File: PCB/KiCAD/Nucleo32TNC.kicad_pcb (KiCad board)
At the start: 2 copper layers, 66 x 99 mm, 54 parts, among them J1 SJ-43515TS, Q1 2N7000, Q2 2N7000, SW1 PTS645VL58-2 LFS, U1 MCP6004, U2 24LC32

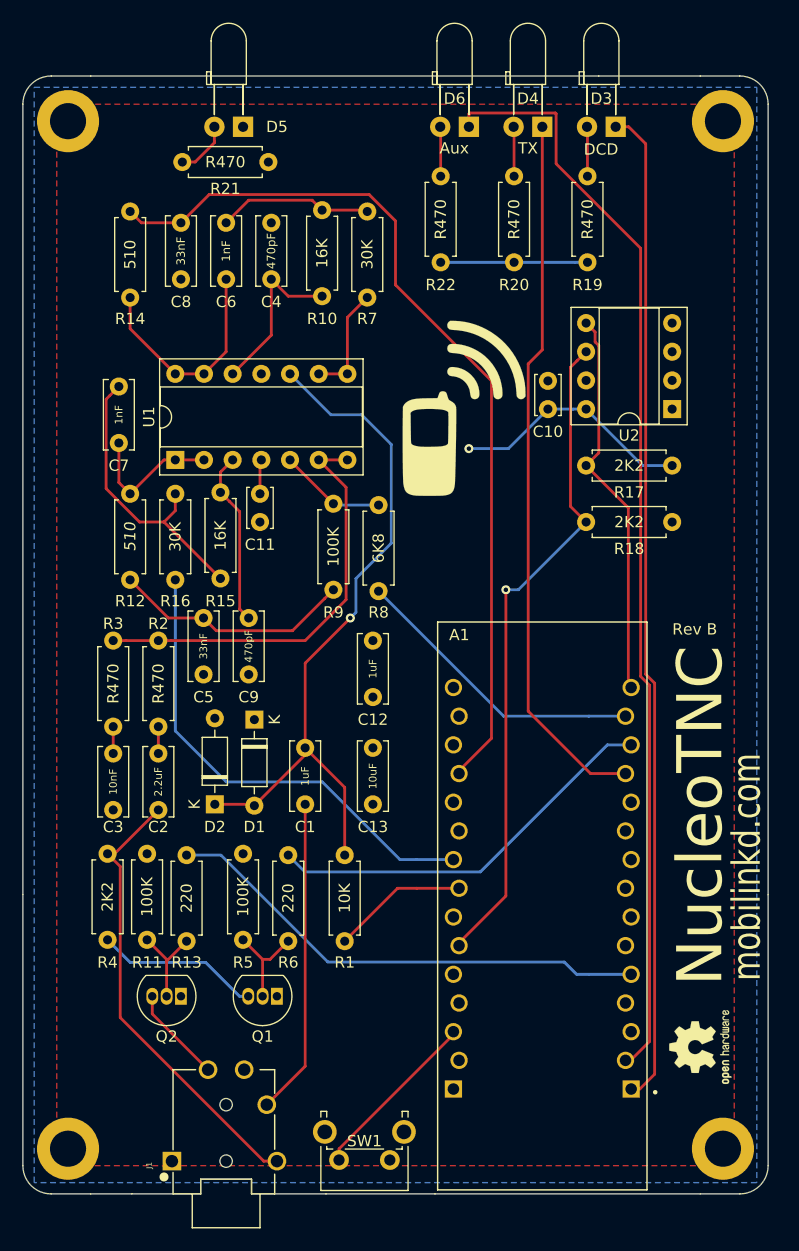
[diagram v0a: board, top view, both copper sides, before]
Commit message: Update placement of *.SilkS
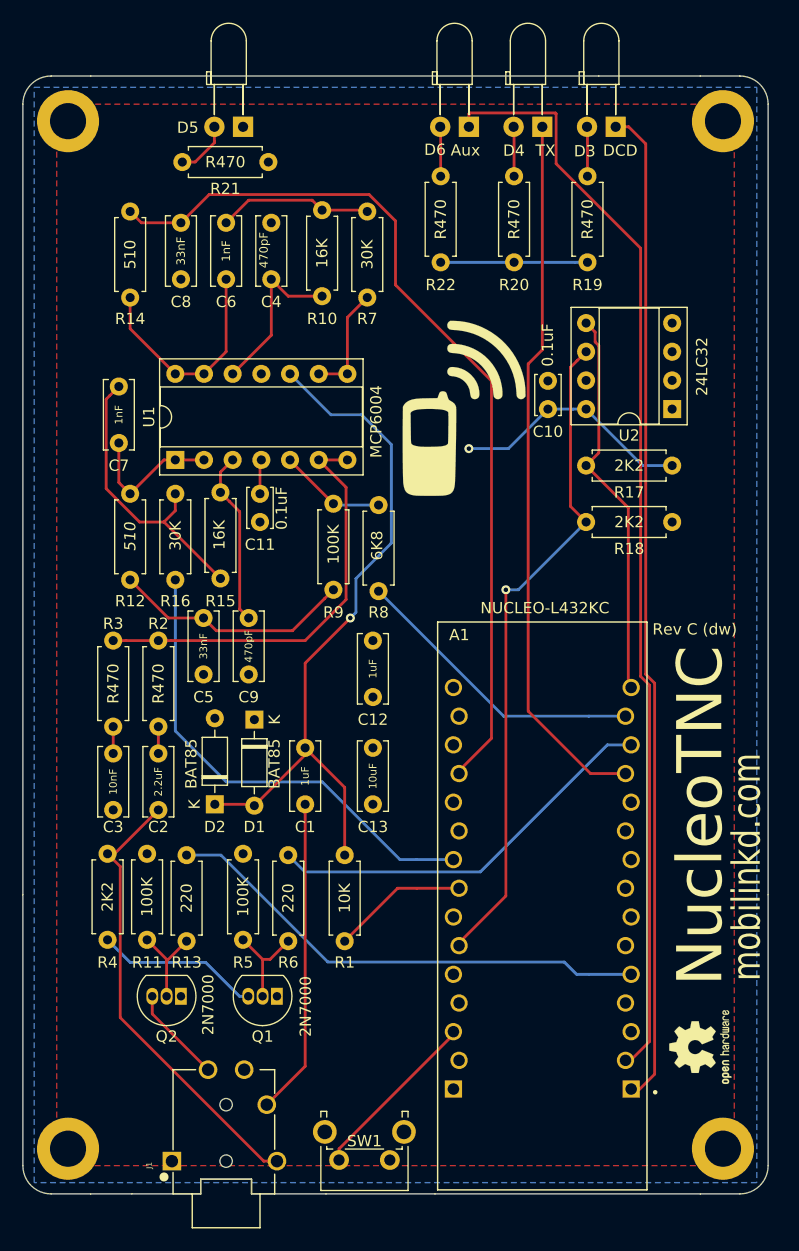
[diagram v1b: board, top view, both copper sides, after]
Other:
- board text added: "Rev C (dw)"
- board text removed: "Rev B"
